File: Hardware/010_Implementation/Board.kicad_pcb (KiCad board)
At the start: 2 copper layers, 58 parts, among them IC1 SN65HVD233-HT, J1 USB_B_Mini, J2 Conn_01x09_Female, J4 Conn_02x05_Odd_Even, K1 G2R2A, Q1 2N7002, Q2 2N7002, Q3 2N7002, Q4 2N7002, Q5 2N7002, Q6 2N7002, Q7 2N7002, SW1 SW_Push, U1 LT1086-3.3, U10 FDV304P, U11 FDV304P, U12 FDV304P, U13 FDV304P, U14 ESP32-DEVKITC-32D, U2 LM1085-3.3, U3 FDV304P, U4 FDV304P, U5 FDV304P, U6 FDV304P, U7 FDV304P, U8 FDV304P, U9 FDV304P, X1 2716-106

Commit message: Modified Board Schematic. Optimized supply and switching system through Software
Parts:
- removed J4: Conn_02x05_Odd_Even, Connector_PinHeader_1.00mm:PinHeader_2x05_P1.00mm_Vertical
- removed Q2, Q3, Q4, Q5, Q6, Q7: 2N7002, Board:SOT23-3
- removed R16, R17: 220, Resistor_SMD:R_2512_6332Metric_Pad1.52x3.35mm_HandSolder
- removed U10, U11, U12, U13, U3, U4, U5, U6, U7, U8, U9: FDV304P, Board:SOT23-3
- removed U14: ESP32-DEVKITC-32D, Board:MODULE_ESP32-DEVKITC-32D
- added D6: GREEN, LED_THT:LED_D3.0mm, F.Cu at (268.1, 118.2)
- added D7: RED, LED_THT:LED_D3.0mm, F.Cu at (183.3, 139.2)
- added D8: 1N4148, Diode_THT:D_DO-35_SOD27_P7.62mm_Horizontal, F.Cu at (184.0, 117.5)
- added K2: G5V-2-DC5, Board:RELAY_G5V-2-DC5, F.Cu at (162.9, 126.4)
- C1: value 100n -> 10n
- D3: value LED -> SS24; footprint LED_SMD:LED_1806_4516Metric_Pad1.57x1.80mm_HandSolder -> Board:DIOM5336X265N
- D4: value LED -> RED; footprint LED_SMD:LED_1806_4516Metric_Pad1.57x1.80mm_HandSolder -> LED_THT:LED_D3.0mm
- D5: value LED -> GREEN; footprint LED_SMD:LED_1806_4516Metric_Pad1.57x1.80mm_HandSolder -> LED_THT:LED_D3.0mm
- J1: value USB_B_Mini -> Conn_02x05_Odd_Even; footprint Connector_USB:USB_Micro-B_Wuerth_629105150521_CircularHoles -> Connector_PinHeader_1.00mm:PinHeader_2x05_P1.00mm_Vertical
- K1: value G2R2A -> G5V-2-DC5; footprint Board:G2R2A -> Board:RELAY_G5V-2-DC5
- Q1: value 2N7002 -> BC817; footprint Board:SOT23-3 -> Package_TO_SOT_SMD:SOT-23
- R1: value 220 -> 1k; footprint Resistor_SMD:R_2512_6332Metric_Pad1.52x3.35mm_HandSolder -> Resistor_SMD:R_0805_2012Metric_Pad1.15x1.40mm_HandSolder
- R10: value 220 -> 500; footprint Resistor_SMD:R_2512_6332Metric_Pad1.52x3.35mm_HandSolder -> Resistor_SMD:R_0805_2012Metric_Pad1.15x1.40mm_HandSolder
- R11, R12, R13: value 100 -> 500; footprint Resistor_SMD:R_2512_6332Metric_Pad1.52x3.35mm_HandSolder -> Resistor_SMD:R_0805_2012Metric_Pad1.15x1.40mm_HandSolder
- R14: value 100 -> 430; footprint Resistor_SMD:R_2512_6332Metric_Pad1.52x3.35mm_HandSolder -> Resistor_SMD:R_0805_2012Metric_Pad1.15x1.40mm_HandSolder
- R15: value 220 -> 150; footprint Resistor_SMD:R_2512_6332Metric_Pad1.52x3.35mm_HandSolder -> Resistor_SMD:R_0805_2012Metric_Pad1.15x1.40mm_HandSolder
- R2, R6, R7: value 220 -> 100; footprint Resistor_SMD:R_2512_6332Metric_Pad1.52x3.35mm_HandSolder -> Resistor_SMD:R_0805_2012Metric_Pad1.15x1.40mm_HandSolder
- R3, R4: value 220 -> 62; footprint Resistor_SMD:R_2512_6332Metric_Pad1.52x3.35mm_HandSolder -> Resistor_SMD:R_0805_2012Metric_Pad1.15x1.40mm_HandSolder
- R5: value 220 -> 2.2k; footprint Resistor_SMD:R_2512_6332Metric_Pad1.52x3.35mm_HandSolder -> Resistor_SMD:R_0805_2012Metric_Pad1.15x1.40mm_HandSolder
- R8, R9: value 62 -> 100; footprint Resistor_SMD:R_2512_6332Metric_Pad1.52x3.35mm_HandSolder -> Resistor_SMD:R_0805_2012Metric_Pad1.15x1.40mm_HandSolder
- U1: value LT1086-3.3 -> LT1086-5.0; footprint Package_TO_SOT_SMD:TO-263-3_TabPin4 -> Board:DPAK254P1394X457-4N
- U2: value LM1085-3.3 -> ESP32-DEVKITC-32D; footprint Package_TO_SOT_SMD:TO-263-3_TabPin4 -> Board:MODULE_ESP32-DEVKITC-32D
- X1: footprint Board:P-804-106 -> Board:P-2716-106; moved to B.Cu
- moved U2 230.9 mm to (254.5, 146.9)
- moved R5 208.1 mm to (218.4, 141.0)
- moved C1 203.5 mm to (218.9, 130.3), turned to 270 degrees
- moved R11 203.3 mm to (274.4, 123.1), turned to 270 degrees
- moved R12 200.0 mm to (268.1, 123.1), turned to 270 degrees
- moved R10 196.5 mm to (280.8, 123.1), turned to 270 degrees
- moved U1 186.6 mm to (192.5, 128.4), turned to 0 degrees
- moved R6 185.6 mm to (204.0, 124.7), turned to 180 degrees
- moved C2 183.3 mm to (210.5, 140.1)
- moved X1 182.4 mm to (253.4, 129.5)
- moved C6 182.3 mm to (216.5, 158.1), turned to 0 degrees
- moved D4 179.1 mm to (280.8, 118.2), turned to 90 degrees
- moved R7 178.6 mm to (204.0, 128.3)
- moved K1 178.3 mm to (175.3, 126.4), turned to 270 degrees
- moved J1 176.9 mm to (213.2, 131.8)
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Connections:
- C1 pad 1: Net-(C1-Pad1) -> /MCU/OBD_Voltage_Check
- C2 pad 1: VCC -> /Connector/OBD_VDD
- C3 pad 1: /CAN_Transceiver/CAN_H -> /CAN_Transceiver/BUS_H
- C4 pad 1: /CAN_Transceiver/OBD_L -> /CAN_Transceiver/BUS_L
- C7 pad 1: Net-(C7-Pad1) -> /MCU/WiFi_Mode
- D1 pad 2: /CAN_Transceiver/CAN_H -> /CAN_Transceiver/BUS_H
- D2 pad 2: /CAN_Transceiver/OBD_L -> /CAN_Transceiver/BUS_L
- D4 pad 1: /MCU/Ind_AP_Mode -> Net-(D4-Pad1)
- D4 pad 2: Net-(D4-Pad2) -> /MCU/Indicator_Error
- D5 pad 1: /MCU/Ind_STA_Mode -> Net-(D5-Pad1)
- D5 pad 2: Net-(D5-Pad2) -> /MCU/Indicator_AP_Mode
- IC1 pad 3: VCC -> +3V3
- IC1 pad 5: /CAN_Transceiver/EN_Transceiver -> GND
- J1 pad 1: Net-(J1-Pad1) -> +3V3
- J1 pad 3: Net-(J1-Pad3) -> GND
- J2 pad 1: Net-(J2-Pad1) -> (no net)
- J2 pad 2: /CAN_Transceiver/OBD_GND -> /Connector/Pin_2
- J2 pad 3: /CAN_Transceiver/CAN_GND -> /Connector/Pin_3
- J2 pad 4: Net-(J2-Pad4) -> (no net)
- J2 pad 5: /CAN_Transceiver/OBD_L -> /Connector/Pin_5
- J2 pad 6: Net-(J2-Pad6) -> (no net)
- J2 pad 7: /CAN_Transceiver/CAN_H -> /Connector/Pin_7
- J2 pad 8: Net-(J2-Pad8) -> (no net)
- J2 pad 9: /CAN_Transceiver/OBD_VDD -> /Connector/OBD_VDD
- K1 pad 1: /CAN_Transceiver/OBD_VDD -> Net-(D8-Pad2)
- L1 pad 2: /CAN_Transceiver/CAN_H -> /CAN_Transceiver/BUS_H
- L1 pad 4: /CAN_Transceiver/OBD_L -> /CAN_Transceiver/BUS_L
- Q1 pad 3: Net-(Q1-Pad3) -> Net-(D8-Pad2)
- R1 pad 1: /CAN_Transceiver/EN_CAN -> /Connector/OBD_VDD
- R1 pad 2: Net-(Q1-Pad1) -> /MCU/OBD_Voltage_Check
- R10 pad 1: /MCU/WiFi_Mode -> Net-(D4-Pad1)
- R10 pad 2: Net-(C7-Pad1) -> GND
- R11 pad 1: Net-(J4-Pad8) -> Net-(D5-Pad1)
- R11 pad 2: /MCU/MTDI -> GND
- R12 pad 2: /MCU/MTDO -> GND
- R13 pad 2: /MCU/MTCK -> /Connector/CAN_Mode
- R14 pad 1: Net-(J4-Pad2) -> Net-(Q1-Pad1)
- R14 pad 2: /MCU/MTMS -> /Connector/OBD-CAN_Switch
- R15 pad 1: GND -> Net-(Q1-Pad1)
- R15 pad 2: Net-(D3-Pad2) -> GND
- R2 pad 1: Net-(R2-Pad1) -> /MCU/OBD_Voltage_Check
- R2 pad 2: Net-(Q1-Pad3) -> GND
- R3 pad 1: /Power Supply/USB_MF_Switch/EN_2 -> Net-(C5-Pad1)
- R3 pad 2: Net-(Q2-Pad3) -> Net-(C6-Pad1)
- R4 pad 1: Net-(R4-Pad1) -> Net-(C6-Pad1)
- R4 pad 2: Net-(Q3-Pad3) -> Net-(C5-Pad2)
- R5 pad 1: /MCU/USB_VDD -> +3V3
- R5 pad 2: Net-(Q4-Pad3) -> /MCU/WiFi_Mode
- R6 pad 1: Net-(R6-Pad1) -> Net-(J1-Pad8)
- R6 pad 2: Net-(Q6-Pad3) -> /MCU/MTDI
- R7 pad 1: /CAN_Transceiver/EN_CAN -> Net-(J1-Pad6)
- R7 pad 2: GND -> /MCU/MTDO
- R8 pad 1: Net-(C5-Pad1) -> Net-(J1-Pad4)
- R8 pad 2: Net-(C6-Pad1) -> /MCU/MTCK
- R9 pad 1: Net-(C6-Pad1) -> Net-(J1-Pad2)
- R9 pad 2: Net-(C5-Pad2) -> /MCU/MTMS
- SW1 pad 1: /MCU/WiFi_Mode -> GND
- SW1 pad 2: VCC -> /MCU/WiFi_Mode
- U1 pad 2: /CAN_Transceiver/EN_CAN -> /MCU/Ext.5V
- U1 pad 3: Net-(C1-Pad1) -> /Connector/OBD_VDD
- U2 pad 1: GND -> +3V3
- U2 pad 2: /Power Supply/USB_MF_Switch/EN_2 -> (no net)
- U2 pad 3: Net-(J1-Pad1) -> (no net)
- X1 pad L1.1: /MCU/USB_VDD -> (no net)
- X1 pad L1.2: /MCU/USB_VDD -> /MCU/GPIO_1
- X1 pad L2.1: GND -> (no net)
- X1 pad L2.2: GND -> /MCU/GPIO_2
- X1 pad L3.1: /MCU/GPIO_1 -> (no net)
- X1 pad L3.2: /MCU/GPIO_1 -> /MCU/GPIO_3
- X1 pad L4.1: /MCU/GPIO_2 -> (no net)
- X1 pad L4.2: /MCU/GPIO_2 -> /MCU/GPIO_4
- X1 pad L5.1: /MCU/GPIO_3 -> (no net)
- X1 pad L5.2: /MCU/GPIO_3 -> GND
- X1 pad L6.1: /MCU/GPIO_4 -> (no net)
- X1 pad L6.2: /MCU/GPIO_4 -> +3V3
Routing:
- net GND: track 468.3 -> 0.00 mm, vias 4 -> 0
- net VCC: track 168.7 -> 0.00 mm, vias 3 -> 0
- net /MCU/USB_VDD: track 141.9 -> 0.00 mm, vias 1 -> 0
- net /CAN_Transceiver/EN_CAN: track 133.4 -> 0.00 mm, vias 3 -> 0
- net /CAN_Transceiver/OBD_L: track 93.0 -> 0.00 mm
- net /CAN_Transceiver/OBD_GND: track 89.9 -> 0.00 mm
- net /CAN_Transceiver/CAN_H: track 83.8 -> 0.00 mm
- net /MCU/GPIO_4: track 82.0 -> 0.00 mm
- net /MCU/GPIO_1: track 77.5 -> 0.00 mm
- net /MCU/GPIO_3: track 76.2 -> 0.00 mm
- net /MCU/WiFi_Mode: track 74.2 -> 0.00 mm
- net /MCU/GPIO_2: track 71.4 -> 0.00 mm
- net /MCU/MTDI: track 65.0 -> 0.00 mm, vias 1 -> 0
- net /Power Supply/USB_MF_Switch/EN_2: track 63.8 -> 0.00 mm, vias 3 -> 0
- net Net-(Q1-Pad1): track 54.9 -> 0.00 mm
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
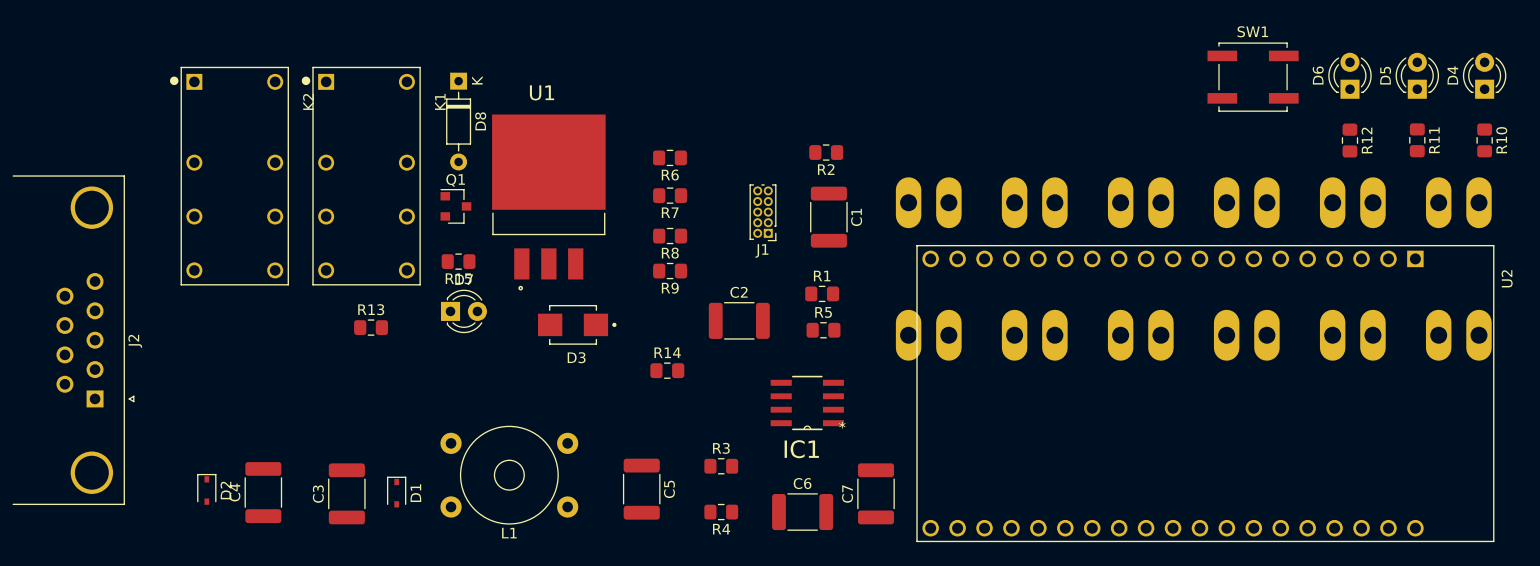
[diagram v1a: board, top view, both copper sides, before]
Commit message: Added Schotlly Diode, PDF and autorouted Vias
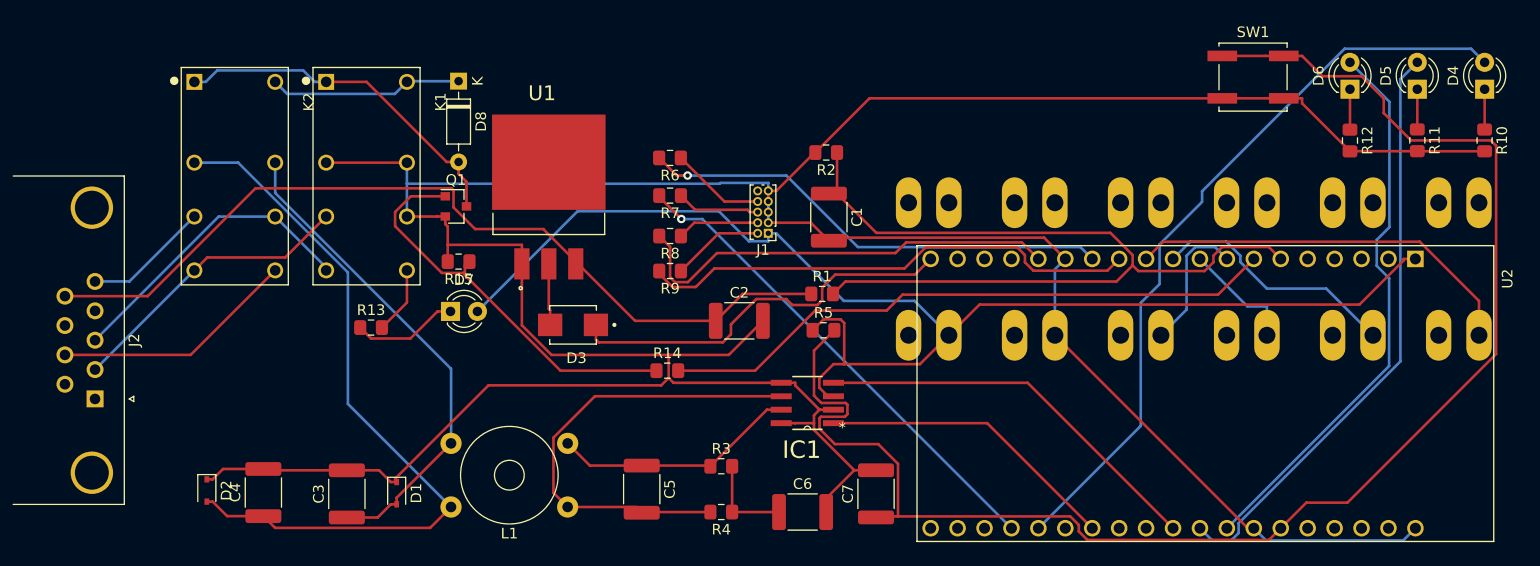
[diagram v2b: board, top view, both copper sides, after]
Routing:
- net GND: track 0.00 -> 337.4 mm
- net /MCU/WiFi_Mode: track 0.00 -> 145.7 mm
- net +3V3: track 0.00 -> 125.2 mm
- net /Connector/OBD_VDD: track 0.00 -> 82.0 mm
- net /MCU/OBD_Voltage_Check: track 0.00 -> 81.2 mm
- net /MCU/Indicator_Error: track 0.00 -> 70.9 mm
- net /CAN_Transceiver/BUS_L: track 0.00 -> 69.8 mm
- net /Connector/OBD-CAN_Switch: track 0.00 -> 58.7 mm
- net /MCU/Indicator_AP_Mode: track 0.00 -> 55.8 mm
- net /MCU/Indicator_STA_Mode: track 0.00 -> 52.8 mm
- net /MCU/MTMS: track 0.00 -> 47.5 mm
- net /CAN_Transceiver/BUS_H: track 0.00 -> 46.4 mm
- net /MCU/MTDO: track 0.00 -> 46.3 mm, vias 0 -> 1
- net /MCU/MTDI: track 0.00 -> 44.8 mm, vias 0 -> 1
- net Net-(C5-Pad2): track 0.00 -> 43.9 mm
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
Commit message: PCB Updated
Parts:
- removed D2: SD05_SOD323, Diode_SMD:D_SOD-323
- D1: value SD05_SOD323 -> PESD1CAN; footprint Diode_SMD:D_SOD-323 -> Board:SOT23-3
- moved R10 224.2 mm to (77.7, 28.1), turned to 90 degrees
- moved D4 220.3 mm to (77.7, 32.9), turned to 270 degrees
- moved R11 212.8 mm to (84.1, 28.1), turned to 90 degrees
- moved D5 208.6 mm to (84.1, 32.9), turned to 270 degrees
- moved R12 201.5 mm to (90.4, 28.1), turned to 90 degrees
- moved D6 197.1 mm to (90.4, 32.9), turned to 270 degrees
- moved U1 181.0 mm to (39.7, 31.4), turned to 90 degrees
- moved SW1 179.7 mm to (99.6, 34.0), turned to 0 degrees
- moved J1 179.1 mm to (65.8, 30.1), turned to 0 degrees
- moved C7 179.1 mm to (86.6, 40.9), turned to 180 degrees
- moved R1 178.2 mm to (67.2, 43.2), turned to 270 degrees
- moved R14 172.4 mm to (67.1, 39.8)
- moved R2 170.5 mm to (66.9, 46.6)
- moved C6 169.9 mm to (87.2, 47.8), turned to 90 degrees
- moved C2 169.8 mm to (73.0, 40.5)
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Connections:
- D1 pad 1: GND -> /CAN_Transceiver/BUS_H
- D1 pad 2: /CAN_Transceiver/BUS_H -> /CAN_Transceiver/BUS_L
- D3 pad A: /MCU/Ext.5V -> +5V
- D8 pad 1: Net-(D8-Pad1) -> +5V
- J2 pad 0: (no net) -> GND
- K1 pad 16: Net-(D8-Pad1) -> +5V
- K2 pad 16: Net-(D8-Pad1) -> +5V
- U1 pad 2: /MCU/Ext.5V -> +5V
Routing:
- net +5V: track 0.00 -> 78.0 mm
- net /MCU/WiFi_Mode: track 145.7 -> 69.6 mm
- net /MCU/GPIO_3: track 10.9 -> 68.2 mm
- net /MCU/GPIO_4: track 13.1 -> 59.8 mm
- net /CAN_Transceiver/BUS_L: track 69.8 -> 26.3 mm
- net Net-(C5-Pad2): track 43.9 -> 18.3 mm
- net Net-(Q1-Pad1): track 38.3 -> 13.9 mm
- net /MCU/Indicator_Error: track 70.9 -> 46.7 mm
- net +3V3: track 125.2 -> 148.8 mm, vias 0 -> 1
- net /Connector/CAN_Mode: track 6.37 -> 29.7 mm
- net Net-(D8-Pad2): track 33.4 -> 54.9 mm
- net GND: track 337.4 -> 358.2 mm, vias 0 -> 44
- net Net-(D8-Pad1): track 18.3 -> 0.00 mm
- net /Connector/OBD-CAN_Switch: track 58.7 -> 76.9 mm
- net /CAN_Transceiver/CAN_Rx: track 37.7 -> 55.9 mm
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- added copper zone on B.Cu, net GND
- added copper zone on F.Cu, net GND

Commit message: Board version 4
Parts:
- removed the R15 at (60.8, 35.4)
- removed X1: 2716-106, Board:P-2716-106
- added C3: 22u, Capacitor_SMD:C_0603_1608Metric_Pad1.05x0.95mm_HandSolder, F.Cu at (133.3, 120.0)
- added J1: 2606-3356, Board:2606-3356, B.Cu at (224.9, 116.8)
- added L2: 744242220, SamacSys_Parts:WE-SLM77, B.Cu at (147.5, 125.7)
- added R18: 150, Resistor_SMD:R_0805_2012Metric_Pad1.15x1.40mm_HandSolder, F.Cu at (143.4, 137.2)
- added R3: 100k, Resistor_SMD:R_0805_2012Metric_Pad1.15x1.40mm_HandSolder, F.Cu at (129.3, 120.0)
- added R4: 0, Resistor_SMD:R_0603_1608Metric_Pad1.05x0.95mm_HandSolder, B.Cu at (148.1, 121.3)
- added R5: 0, Resistor_SMD:R_0603_1608Metric_Pad1.05x0.95mm_HandSolder, B.Cu at (147.2, 128.9)
- C1: footprint Capacitor_SMD:C_1812_4532Metric_Pad1.30x3.40mm_HandSolder -> Capacitor_SMD:C_0603_1608Metric_Pad1.05x0.95mm_HandSolder
- C2: value 100n -> 10u; footprint Capacitor_SMD:C_1812_4532Metric_Pad1.30x3.40mm_HandSolder -> Capacitor_SMD:C_0603_1608Metric_Pad1.05x0.95mm_HandSolder
- C4: renamed from C3; footprint Capacitor_SMD:C_1812_4532Metric_Pad1.30x3.40mm_HandSolder -> Capacitor_SMD:C_0603_1608Metric_Pad1.05x0.95mm_HandSolder; moved to B.Cu
- C5: renamed from C4; footprint Capacitor_SMD:C_1812_4532Metric_Pad1.30x3.40mm_HandSolder -> Capacitor_SMD:C_0603_1608Metric_Pad1.05x0.95mm_HandSolder; moved to B.Cu
- C6: renamed from C5; footprint Capacitor_SMD:C_1812_4532Metric_Pad1.30x3.40mm_HandSolder -> Capacitor_SMD:C_0603_1608Metric_Pad1.05x0.95mm_HandSolder; moved to B.Cu
- C7: renamed from C6; footprint Capacitor_SMD:C_1812_4532Metric_Pad1.30x3.40mm_HandSolder -> Capacitor_SMD:C_0603_1608Metric_Pad1.05x0.95mm_HandSolder; moved to B.Cu
- C8: renamed from C7; footprint Capacitor_SMD:C_1812_4532Metric_Pad1.30x3.40mm_HandSolder -> Capacitor_SMD:C_0603_1608Metric_Pad1.05x0.95mm_HandSolder
- D1: moved to B.Cu
- L1: value L_Core_Ferrite_Coupled -> 2.2u; footprint Transformer_THT:Transformer_Toroid_Horizontal_D9.0mm_Amidon-T30 -> Capacitor_SMD:C_0603_1608Metric_Pad1.05x0.95mm_HandSolder
- R1: value 1k -> 10k
- R2: value 100 -> 1k
- R6: renamed from R3; moved to B.Cu
- R7: renamed from R4; moved to B.Cu
- U1: value LT1086-5.0 -> TPS62163DGK; footprint Board:DPAK254P1394X457-4N -> Package_SO:VSSOP-8_3.0x3.0mm_P0.65mm
- moved R14 144.8 mm to (167.2, 146.7), turned to 180 degrees
- moved D4 144.0 mm to (172.2, 146.7), turned to 0 degrees
- moved D7 143.8 mm to (131.6, 146.7), turned to 0 degrees
- moved Q1 138.4 mm to (143.7, 141.0), turned to 270 degrees
- moved R13 135.2 mm to (143.7, 146.1), turned to 180 degrees
- moved R16 134.5 mm to (120.8, 146.7)
- moved J2 133.9 mm to (148.8, 135.3)
- moved R15 133.9 mm to (167.2, 137.8), turned to 180 degrees
- moved R9 133.8 mm to (155.4, 140.7)
- moved R10 133.8 mm to (155.4, 138.6)
- moved R11 133.8 mm to (155.4, 136.3)
- moved R12 133.8 mm to (155.4, 134.1)
- moved D3 133.6 mm to (148.8, 146.1), turned to 0 degrees
- moved D5 133.0 mm to (172.2, 137.8), turned to 0 degrees
- moved D6 131.3 mm to (124.6, 146.7), turned to 0 degrees
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- renumbered D3 to D2, D4 to D3, D5 to D4, D6 to D5, D7 to D6, D8 to D7, J1 to J2, J2 to J3, R7 to R10, R8 to R11, R9 to R12, R10 to R13, R11 to R14, R12 to R15, R13 to R16, R14 to R17, R5 to R8, R6 to R9
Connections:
- C6 pad 1: Net-(C5-Pad1) -> Net-(C6-Pad1)
- C6 pad 2: Net-(C5-Pad2) -> Net-(C6-Pad2)
- D2 pad C: Net-(D3-PadC) -> Net-(D2-PadC)
- IC1 pad 6: Net-(C5-Pad2) -> Net-(C6-Pad2)
- IC1 pad 7: Net-(C5-Pad1) -> Net-(C6-Pad1)
- L1 pad 1: Net-(C5-Pad1) -> Net-(L1-Pad1)
- L1 pad 2: /CAN_Transceiver/BUS_H -> +5V
- R6 pad 1: Net-(C5-Pad1) -> Net-(C6-Pad1)
- R7 pad 2: Net-(C5-Pad2) -> Net-(C6-Pad2)
- U1 pad 2: +5V -> /Connector/OBD_VDD
- U1 pad 4: (no net) -> GND
- U2 pad 1: +3V3 -> (no net)
- U2 pad 10: /MCU/GPIO_2 -> /MCU/GPIO_1
- U2 pad 11: /MCU/GPIO_1 -> /MCU/MTMS
- U2 pad 12: /MCU/MTMS -> /MCU/MTDI
- U2 pad 13: /MCU/MTDI -> GND
- U2 pad 14: GND -> /MCU/MTCK
- U2 pad 15: /MCU/MTCK -> Net-(D2-PadC)
- U2 pad 19: Net-(D3-PadC) -> (no net)
- U2 pad 20: GND -> /MCU/WiFi_Mode
- U2 pad 21: (no net) -> /MCU/Indicator_STA_Mode
- U2 pad 22: (no net) -> /MCU/Indicator_AP_Mode
- U2 pad 23: (no net) -> /CAN_Transceiver/CAN_Rx
- U2 pad 25: /MCU/WiFi_Mode -> (no net)
- U2 pad 26: GND -> /CAN_Transceiver/CAN_Tx
- U2 pad 27: /MCU/Indicator_STA_Mode -> /MCU/Indicator_Error
- U2 pad 28: /MCU/Indicator_AP_Mode -> /MCU/MTDO
- U2 pad 29: /CAN_Transceiver/CAN_Rx -> GND
- U2 pad 30: (no net) -> +3V3
- U2 pad 5: (no net) -> /MCU/OBD_Voltage_Check
- U2 pad 6: /MCU/OBD_Voltage_Check -> /Connector/OBD-CAN_Switch
- U2 pad 7: /Connector/OBD-CAN_Switch -> /MCU/GPIO_4
- U2 pad 8: /MCU/GPIO_4 -> /MCU/GPIO_3
- U2 pad 9: /MCU/GPIO_3 -> /MCU/GPIO_2
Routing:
- net GND: track 358.2 -> 0.00 mm, vias 44 -> 5
- net Net-(D2-PadC): track 0.00 -> 100.5 mm
- net /Connector/OBD_VDD: track 87.2 -> 26.5 mm
- net Net-(D3-PadC): track 55.8 -> 0.00 mm, vias 1 -> 0
- net /MCU/GPIO_3: track 68.2 -> 18.8 mm
- net /MCU/GPIO_4: track 59.8 -> 22.5 mm
- net +3V3: track 148.8 -> 111.9 mm, vias 1 -> 0
- net /MCU/Indicator_Error: track 46.7 -> 75.0 mm
- net /MCU/Indicator_STA_Mode: track 52.9 -> 25.7 mm
- net +5V: track 78.0 -> 52.1 mm
- net /Connector/CAN_Mode: track 29.7 -> 4.23 mm
- net Net-(D7-Pad2): track 54.9 -> 31.4 mm
- net /MCU/MTDO: track 52.8 -> 73.9 mm
- net /CAN_Transceiver/CAN_Rx: track 55.9 -> 35.1 mm
- net /MCU/Indicator_AP_Mode: track 55.9 -> 36.1 mm
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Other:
- board outline added: 123.2 x 44.5 mm

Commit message: Board version 4.1
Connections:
- J1 pad 1: (no net) -> Net-(J1-Pad1)
- J1 pad 11: (no net) -> Net-(J1-Pad11)
- J1 pad 3: (no net) -> Net-(J1-Pad3)
- J1 pad 5: (no net) -> Net-(J1-Pad5)
- J1 pad 7: (no net) -> Net-(J1-Pad7)
- J1 pad 9: (no net) -> Net-(J1-Pad9)
- J2 pad 10: (no net) -> Net-(J2-Pad10)
- J3 pad 0: GND -> (no net)
- J3 pad 1: (no net) -> Net-(J3-Pad1)
- J3 pad 4: (no net) -> Net-(J3-Pad4)
- J3 pad 6: (no net) -> Net-(J3-Pad6)
- J3 pad 8: (no net) -> Net-(J3-Pad8)
- U2 pad 1: (no net) -> Net-(U2-Pad1)
- U2 pad 16: (no net) -> Net-(U2-Pad16)
- U2 pad 17: (no net) -> Net-(U2-Pad17)
- U2 pad 18: (no net) -> Net-(U2-Pad18)
- U2 pad 19: (no net) -> Net-(U2-Pad19)
- U2 pad 2: (no net) -> Net-(U2-Pad2)
- U2 pad 24: (no net) -> Net-(U2-Pad24)
- U2 pad 25: (no net) -> Net-(U2-Pad25)
- U2 pad 3: (no net) -> Net-(U2-Pad3)
- U2 pad 4: (no net) -> Net-(U2-Pad4)
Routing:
- net GND: track 0.00 -> 16.4 mm, vias 5 -> 14
